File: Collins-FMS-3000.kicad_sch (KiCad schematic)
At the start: 26 parts, among them J3 TC2030-IDC-NL, U2 TCA8418, U4 IS31FL3733B

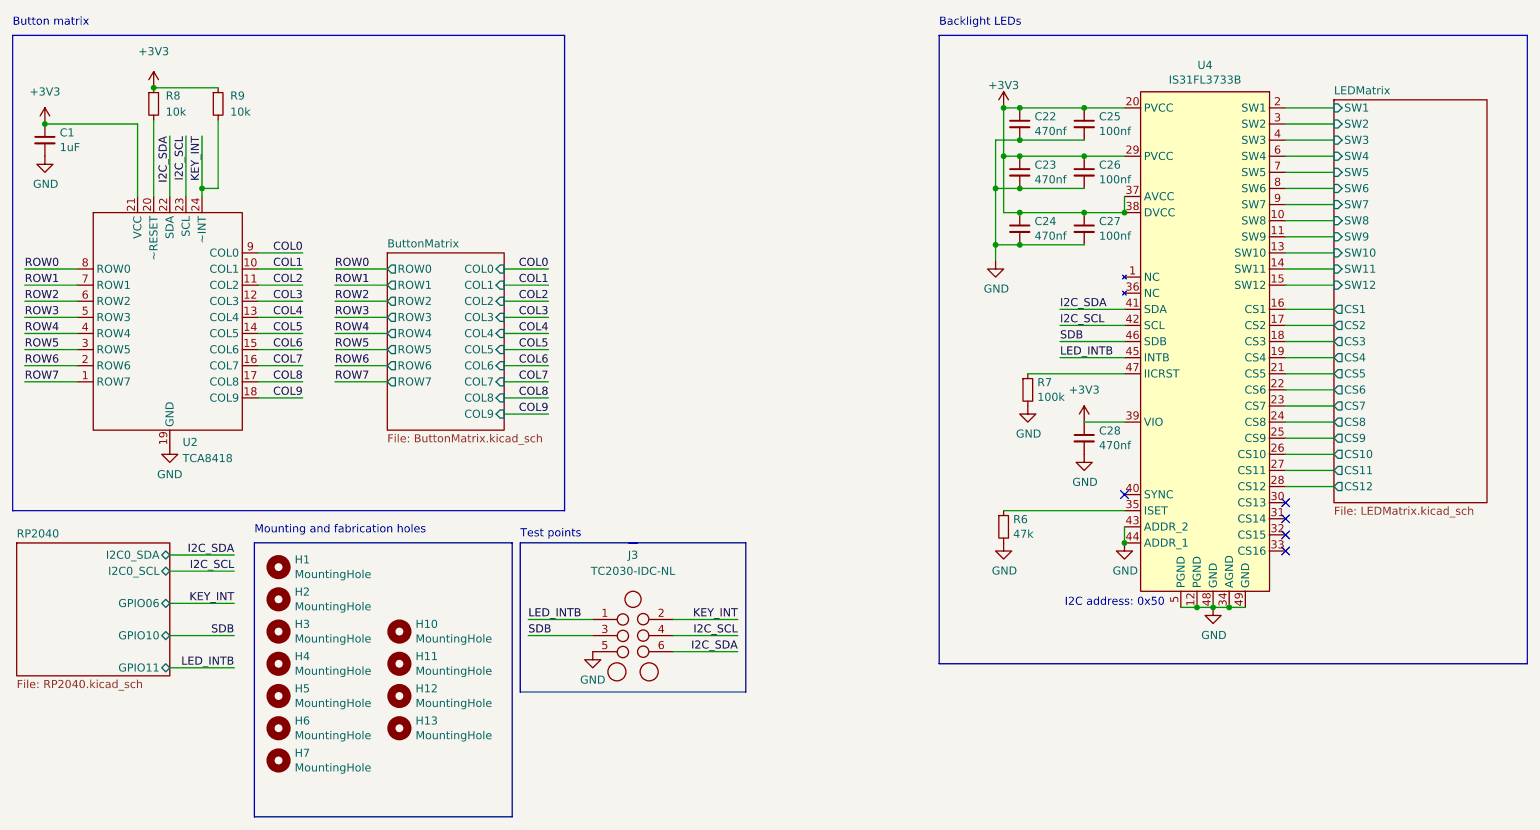
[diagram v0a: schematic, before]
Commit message: New RP2040 layout added
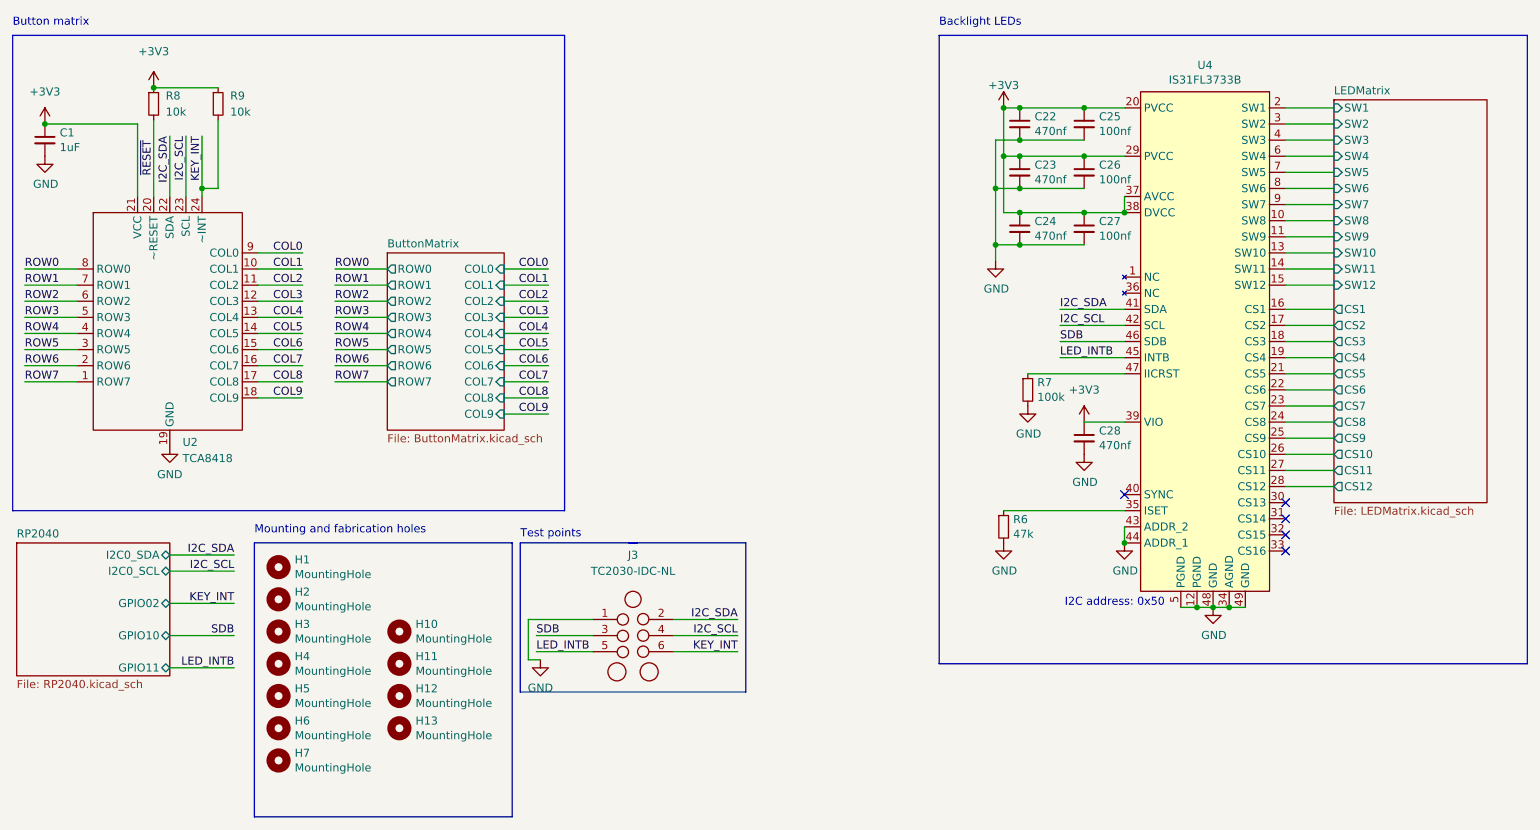
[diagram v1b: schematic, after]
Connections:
- net GND: now also J3.1 (Pin_1); no longer J3.5 (Pin_5)
- net I2C_SDA: now also J3.2 (Pin_2); no longer J3.6 (Pin_6)
- net KEY_INT: now also J3.6 (Pin_6); no longer J3.2 (Pin_2)
- net LED_INTB: now also J3.5 (Pin_5); no longer J3.1 (Pin_1)
- net ~{RESET}: now reaches R8.2, U2.20 (~RESET)
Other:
- sheet RP2040 ports: added GPIO02; removed GPIO06
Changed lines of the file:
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@@
+    (stroke (width 0) (type default) (color 0 0 0 0))
+  )
+  (wire (pts (xy 95.25 108.585) (xy 95.25 114.935))
     (stroke (width 0) (type default) (color 0 0 0 0))
   )
@@
     (stroke (width 0) (type default) (color 0 0 0 0))
   )
-  (wire (pts (xy 105.41 111.125) (xy 95.25 111.125))
-    (stroke (width 0) (type default) (color 0 0 0 0))
-  )
   (wire (pts (xy 15.875 71.12) (xy 24.13 71.12))
     (stroke (width 0) (type default) (color 0 0 0 0))
@@
     (stroke (width 0) (type default) (color 0 0 0 0))
   )
+  (wire (pts (xy 96.52 111.125) (xy 105.41 111.125))
+    (stroke (width 0) (type default) (color 0 0 0 0))
+  )
   (wire (pts (xy 52.705 68.58) (xy 59.69 68.58))
     (stroke (width 0) (type default) (color 0 0 0 0))
@@
     (stroke (width 0) (type default) (color 0 0 0 0))
   )
+  (wire (pts (xy 96.52 113.665) (xy 105.41 113.665))
+    (stroke (width 0) (type default) (color 0 0 0 0))
+  )
   (wire (pts (xy 15.875 68.58) (xy 24.13 68.58))
     (stroke (width 0) (type default) (color 0 0 0 0))
@@
     (stroke (width 0) (type default) (color 0 0 0 0))
   )
+  (wire (pts (xy 95.25 114.935) (xy 97.155 114.935))
+    (stroke (width 0) (type default) (color 0 0 0 0))
+  )
   (wire (pts (xy 189.23 41.91) (xy 189.23 44.45))
     (stroke (width 0) (type default) (color 0 0 0 0))
@@
     (effects (font (size 1.27 1.27)) (justify right bottom))
   )
-  (label "KEY_INT" (at 128.27 108.585 180)
+  (label "I2C_SDA" (at 128.27 108.585 180)
     (effects (font (size 1.27 1.27)) (justify right bottom))
   )
@@
     (effects (font (size 1.27 1.27)) (justify right bottom))
   )
-  (label "I2C_SDA" (at 128.27 113.665 180)
+  (label "KEY_INT" (at 128.27 113.665 180)
     (effects (font (size 1.27 1.27)) (justify right bottom))
   )
@@
     (effects (font (size 1.27 1.27)) (justify left bottom))
   )
-  (label "SDB" (at 95.25 111.125 0)
+  (label "SDB" (at 96.52 111.125 0)
     (effects (font (size 1.27 1.27)) (justify left bottom))
   )
@@
     (effects (font (size 1.27 1.27)) (justify right bottom))
   )
+  (label "~{RESET}" (at 36.195 33.02 270)
+    (effects (font (size 1.27 1.27)) (justify right bottom))
+  )
   (label "COL2" (at 59.69 55.88 180)
     (effects (font (size 1.27 1.27)) (justify right bottom))
@@
     (effects (font (size 1.27 1.27)) (justify left bottom))
   )
-  (label "LED_INTB" (at 95.25 108.585 0)
+  (label "LED_INTB" (at 96.52 113.665 0)
     (effects (font (size 1.27 1.27)) (justify left bottom))
   )
@@
     (pin "6")
   )
-  (symbol (lib_id "power:GND") (at 105.41 113.665 0) (unit 1)
+  (symbol (lib_id "power:GND") (at 97.155 114.935 0) (unit 1)
     (in_bom yes) (on_board yes) (fields_autoplaced)
-    (property "Reference" "#PWR?" (id 0) (at 105.41 120.015 0)
-      (effects (font (size 1.27 1.27)) hide)
-    )
-    (property "Value" "GND" (id 1) (at 105.41 118.11 0))
-    (property "Footprint" "" (id 2) (at 105.41 113.665 0)
-      (effects (font (size 1.27 1.27)) hide)
-    )
-    (property "Datasheet" "" (id 3) (at 105.41 113.665 0)
+    (property "Reference" "#PWR0101" (id 0) (at 97.155 121.285 0)
+      (effects (font (size 1.27 1.27)) hide)
+    )
+    (property "Value" "GND" (id 1) (at 97.155 119.38 0))
+    (property "Footprint" "" (id 2) (at 97.155 114.935 0)
+      (effects (font (size 1.27 1.27)) hide)
+    )
+    (property "Datasheet" "" (id 3) (at 97.155 114.935 0)
       (effects (font (size 1.27 1.27)) hide)
     )
@@
       (effects (font (size 1.27 1.27)) (justify left top))
     )
-    (pin "GPIO06" bidirectional (at 38.735 106.045 0)
+    (pin "GPIO02" bidirectional (at 38.735 106.045 0)
       (effects (font (size 1.27 1.27)) (justify right))
     )
@@
       (reference "#PWR028") (unit 1) (value "GND") (footprint "")
     )
-    (path "/dc0d5261-e4d2-4b54-8008-75fea26fa95d/41b33326-48eb-4de1-92a9-8af053ffde51"
-      (reference "#PWR029") (unit 1) (value "GND") (footprint "")
-    )
     (path "/dc0d5261-e4d2-4b54-8008-75fea26fa95d/8a50b5f7-d609-409d-947b-39530ce2e158"
       (reference "#PWR030") (unit 1) (value "+1V1") (footprint "")
@@
       (reference "#PWR033") (unit 1) (value "+3V3") (footprint "")
     )
-    (path "/dc0d5261-e4d2-4b54-8008-75fea26fa95d/fa5e550a-15ca-428e-9a28-8858ec4b8cc1"
-      (reference "#PWR034") (unit 1) (value "GND") (footprint "")
-    )
     (path "/dc0d5261-e4d2-4b54-8008-75fea26fa95d/1c1eddbd-710f-43b1-b47c-5e4765a94756"
       (reference "#PWR035") (unit 1) (value "GND") (footprint "")
     )
+    (path "/f2888f49-247d-4e90-a5dd-7c723a114c98"
+      (reference "#PWR0101") (unit 1) (value "GND") (footprint "")
+    )
     (path "/0c4a07e0-82f0-4b92-8cb5-34f9de66e922"
       (reference "#PWR0102") (unit 1) (value "+3V3") (footprint "")
@@
       (reference "#PWR0104") (unit 1) (value "GND") (footprint "")
     )
-    (path "/f2888f49-247d-4e90-a5dd-7c723a114c98"
-      (reference "#PWR?") (unit 1) (value "GND") (footprint "")
-    )
     (path "/00000000-0000-0000-0000-0000618b3952"
       (reference "C1") (unit 1) (value "1uF") (footprint "Custom_Footprints:Perfect_0402")
@@
     )
     (path "/dc0d5261-e4d2-4b54-8008-75fea26fa95d/57893719-4e3e-402f-8b67-10cb9a3285f4"
-      (reference "C10") (unit 1) (value "100nF") (footprint "Custom_Footprints:Perfect_0402")
+      (reference "C10") (unit 1) (value "1uF") (footprint "Custom_Footprints:Perfect_0402")
     )
     (path "/dc0d5261-e4d2-4b54-8008-75fea26fa95d/27792339-96aa-456f-97bd-92f46f99c363"
-      (reference "C11") (unit 1) (value "100nF") (footprint "Custom_Footprints:Perfect_0402")
+      (reference "C11") (unit 1) (value "1uF") (footprint "Custom_Footprints:Perfect_0402")
     )
     (path "/dc0d5261-e4d2-4b54-8008-75fea26fa95d/f6ed04a0-ba11-4b67-938a-2ac59d652fb6"
@@
     )
     (path "/dc0d5261-e4d2-4b54-8008-75fea26fa95d/f467e92c-cfec-45d6-9135-43909aa23e31"
-      (reference "C13") (unit 1) (value "100nF") (footprint "Custom_Footprints:Perfect_0402")
-    )
-    (path "/dc0d5261-e4d2-4b54-8008-75fea26fa95d/d60ddee3-3685-41f4-9f86-979901131b67"
+      (reference "C13") (unit 1) (value "1UF") (footprint "Custom_Footprints:Perfect_0402")
+    )
+    (path "/dc0d5261-e4d2-4b54-8008-75fea26fa95d/1a3908e6-1e81-477c-b81d-11898b35bbc6"
       (reference "C14") (unit 1) (value "1uF") (footprint "Custom_Footprints:Perfect_0402")
     )
-    (path "/dc0d5261-e4d2-4b54-8008-75fea26fa95d/1a3908e6-1e81-477c-b81d-11898b35bbc6"
-      (reference "C15") (unit 1) (value "100nF") (footprint "Custom_Footprints:Perfect_0402")
-    )
     (path "/dc0d5261-e4d2-4b54-8008-75fea26fa95d/d8f0cdd3-1d40-4791-9fb1-0cbfb6888f07"
-      (reference "C16") (unit 1) (value "100nF") (footprint "Custom_Footprints:Perfect_0402")
+      (reference "C15") (unit 1) (value "1uF") (footprint "Custom_Footprints:Perfect_0402")
     )
     (path "/dc0d5261-e4d2-4b54-8008-75fea26fa95d/e4c5aa6b-a75e-4fd0-97fb-9ccf912712e8"
-      (reference "C17") (unit 1) (value "100nF") (footprint "Custom_Footprints:Perfect_0402")
+      (reference "C16") (unit 1) (value "1uF") (footprint "Custom_Footprints:Perfect_0402")
     )
     (path "/dc0d5261-e4d2-4b54-8008-75fea26fa95d/9e8cf55f-aa42-463b-a91a-de04527fe165"
-      (reference "C18") (unit 1) (value "100nF") (footprint "Custom_Footprints:Perfect_0402")
+      (reference "C17") (unit 1) (value "1uF") (footprint "Custom_Footprints:Perfect_0402")
     )
     (path "/dc0d5261-e4d2-4b54-8008-75fea26fa95d/f8933443-3eda-49a4-a3dd-e25c75852b5a"
-      (reference "C19") (unit 1) (value "100nF") (footprint "Custom_Footprints:Perfect_0402")
+      (reference "C18") (unit 1) (value "1uF") (footprint "Custom_Footprints:Perfect_0402")
     )
     (path "/dc0d5261-e4d2-4b54-8008-75fea26fa95d/0ebc7e3d-c040-4c6e-aaf8-1870c68a4ff3"
-      (reference "C20") (unit 1) (value "100nF") (footprint "Custom_Footprints:Perfect_0402")
+      (reference "C19") (unit 1) (value "1uF") (footprint "Custom_Footprints:Perfect_0402")
     )
     (path "/00000000-0000-0000-0000-000061946bf2"
